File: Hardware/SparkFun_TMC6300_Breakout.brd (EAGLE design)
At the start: 15.2 x 20.3 mm, 56 parts, among them U2 TMC6300

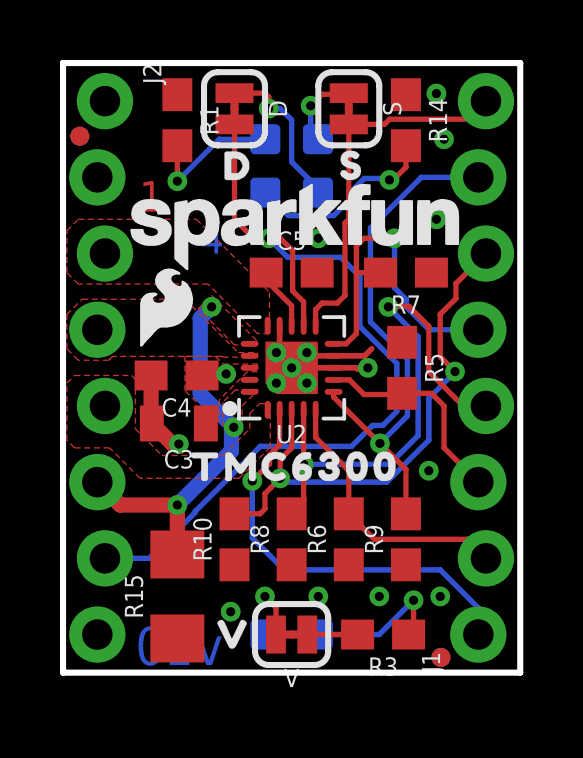
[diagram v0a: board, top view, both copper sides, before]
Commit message: Updates from design review
Changed tCream on the TMC6300 to be reduced by 5%, changed tRestrict polygon to a rectangle, adjusted C5 to match the datasheet for a good return path, adjusted some routing for less acid traps, adjusted ratio of numbers on layers from 15% to 18%, and created a smaller SparkFun logo to fit better on the top side of the board - not 0.08 instead of 0.1
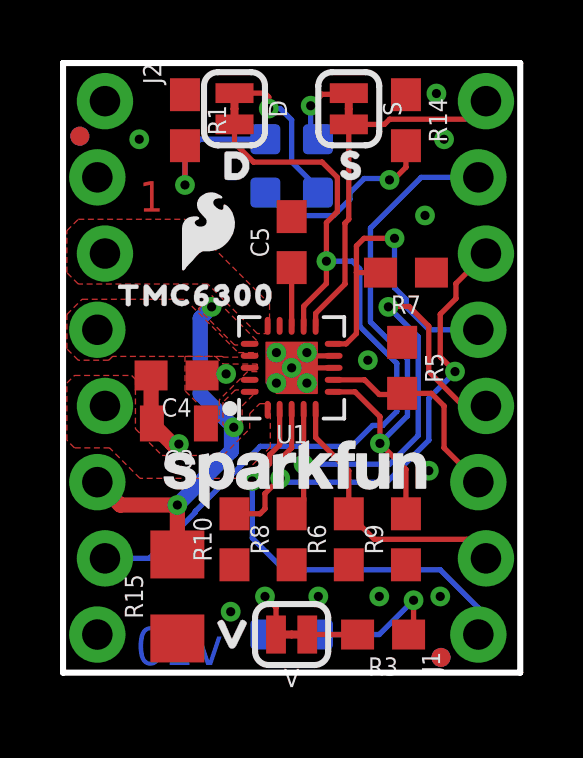
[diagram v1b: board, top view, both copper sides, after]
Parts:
- removed U$17: (no value), output:TMC63000
- added U$4: (no value), output:TMC630063003454
- LOGO3: value SFE_LOGO_NAME.1_INCH -> SFE_LOGO_NAME.08_INCH; device SparkFun-Aesthetics:SFE_LOGO_NAME_.1 -> SparkFun-Aesthetics:SFE_LOGO_NAME_.08
- moved LOGO3 8.13 mm to (7.62, 6.73)
- moved LOGO4 2.90 mm to (4.83, 14.7)
- moved C5 1.02 mm to (7.62, 14.4), turned to 90 degrees
- moved R1 0.25 mm to (4.06, 18.4)
- renumbered U2 to U1
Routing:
- net GND: track 8.12 -> 4.16 mm
- net N$10: track 4.69 -> 5.21 mm

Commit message: Updated production files
Re generated panelized files for ordering from design review changes
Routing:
- net GND: vias 16 -> 17
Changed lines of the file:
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@@
 <wire x1="8.236" y1="10.56" x2="8.128" y2="10.668" width="0.1778" layer="1"/>
 <via x="2.54" y="17.78" extent="1-16" drill="0.3048"/>
+<via x="6.223" y="14.859" extent="1-16" drill="0.3048"/>
 </signal>
 <signal name="N$1">

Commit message: Final updates before ordering
Adjusted GND traces from TMC6300 for better connection, added paragraph for Power LED in schematic, updated panelized files for ordering.
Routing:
- net GND: track 4.16 -> 5.40 mm
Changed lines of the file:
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@@
 <layer number="29" name="tStop" color="7" fill="3" visible="no" active="yes"/>
 <layer number="30" name="bStop" color="7" fill="6" visible="no" active="yes"/>
-<layer number="31" name="tCream" color="7" fill="4" visible="yes" active="yes"/>
+<layer number="31" name="tCream" color="7" fill="4" visible="no" active="yes"/>
 <layer number="32" name="bCream" color="7" fill="5" visible="no" active="yes"/>
 <layer number="33" name="tFinish" color="6" fill="3" visible="no" active="yes"/>
@@
 <layer number="45" name="Holes" color="7" fill="1" visible="yes" active="yes"/>
 <layer number="46" name="Milling" color="3" fill="1" visible="yes" active="yes"/>
-<layer number="47" name="Measures" color="7" fill="1" visible="yes" active="yes"/>
+<layer number="47" name="Measures" color="7" fill="1" visible="no" active="yes"/>
 <layer number="48" name="Document" color="7" fill="1" visible="no" active="yes"/>
 <layer number="49" name="Reference" color="46" fill="1" visible="no" active="yes"/>
@@
 <via x="2.54" y="17.78" extent="1-16" drill="0.3048"/>
 <via x="6.223" y="14.859" extent="1-16" drill="0.3048"/>
+<wire x1="9.02" y1="10.56" x2="9.633" y2="10.56" width="0.1778" layer="1"/>
+<wire x1="9.02" y1="10.16" x2="9.652" y2="10.16" width="0.1778" layer="1"/>
 </signal>
 <signal name="N$1">
